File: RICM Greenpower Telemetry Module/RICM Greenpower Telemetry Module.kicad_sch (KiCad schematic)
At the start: 43 parts, among them J1 Conn_02x04_Counter_Clockwise, J10 Conn_01x02_Female, J11 Conn_01x02_Female, J2 Conn_01x05_Female, J3 Conn_01x02_Female, J4 Conn_01x03_Female, J5 Jack-DC, J6 Conn_01x03_Female, J7 Conn_01x04_Female, J8 Conn_01x02_Female, J9 Conn_01x02_Female, U1 MPU_6050_module, U2 Pico, U3 Adafruit_MicroSD_SPI_SDIO, U4 SI-8050TFE, U5 ADS7830

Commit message: tightened up spacing on the board
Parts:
- removed F1: Polyfuse, Capacitor_THT:C_Disc_D5.0mm_W2.5mm_P5.00mm, symbol Device:Polyfuse
- removed U4: SI-8050TFE, Package_TO_SOT_THT:TO-220-5_P3.4x3.7mm_StaggerOdd_Lead3.8mm_Vertical, symbol Regulator_Switching:SI-8050TFE
- added C1: C, Capacitor_THT:C_Disc_D5.0mm_W2.5mm_P5.00mm, symbol Device:C
- added U1: XL2001E1, Package_SO:SO-8_5.3x6.2mm_P1.27mm, symbol Power_Management:XL2001E1
- renumbered C1 to C2, C2 to C3, C3 to C4, C4 to C5, C5 to C6, J5 to J1, J3 to J11, J1 to J3, J6 to J5, J9 to J6, J11 to J7, J7 to J9, R11 to R10, R12 to R11, R13 to R12, R14 to R13, R18 to R14, R20 to R15, R17 to R16, R6 to R17, R8 to R18, R7 to R19, R9 to R20, R10 to R6, R16 to R7, R19 to R8, R15 to R9, U1 to U3, U3 to U4
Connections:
- net +5V: now also U1.1 (FB)
- net GND: now also U1.7 (GND), U1.8 (GND)
- net at C2.1: now also J1.1, C1.2, U1.4 (VIN)
- net at L1.1: now also U1.5 (SW), U1.6 (SW)
- new net: C1.1, U1.3 (VC)
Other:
- moved on the sheet: C2, C3, J1, L1

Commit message: last revisions before first order
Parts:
- added C7, C8: C, Capacitor_THT:C_Disc_D5.0mm_W2.5mm_P5.00mm, symbol Device:C
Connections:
- net +5V: now also U5.10 (REFin/REFout), C7.1, C8.1
- net GND: now also C7.2, C8.2
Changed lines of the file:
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@@
   (junction (at 137.16 29.21) (diameter 0) (color 0 0 0 0)
   )
+  (junction (at 187.96 121.92) (diameter 0) (color 0 0 0 0)
+  )
   (junction (at 33.02 146.05) (diameter 0) (color 0 0 0 0)
   )
@@
   (junction (at 55.88 143.51) (diameter 0) (color 0 0 0 0)
   )
+  (junction (at 200.66 152.4) (diameter 0) (color 0 0 0 0)
+  )
+  (junction (at 209.55 144.78) (diameter 0) (color 0 0 0 0)
+  )
   (junction (at 78.74 91.44) (diameter 0) (color 0 0 0 0)
   )
@@
   (junction (at 138.43 116.84) (diameter 0) (color 0 0 0 0)
   )
+  (junction (at 218.44 137.16) (diameter 0) (color 0 0 0 0)
+  )
   (junction (at 58.42 151.13) (diameter 0) (color 0 0 0 0)
   )
@@
   (junction (at 107.95 53.34) (diameter 0) (color 0 0 0 0)
   )
+  (junction (at 209.55 137.16) (diameter 0) (color 0 0 0 0)
+  )
   (junction (at 67.31 66.04) (diameter 0) (color 0 0 0 0)
   )
@@
     (stroke (width 0) (type default) (color 0 0 0 0))
   )
+  (wire (pts (xy 209.55 144.78) (xy 218.44 144.78))
+    (stroke (width 0) (type default) (color 0 0 0 0))
+  )
   (wire (pts (xy 59.69 71.12) (xy 69.85 71.12))
     (stroke (width 0) (type default) (color 0 0 0 0))
@@
     (stroke (width 0) (type default) (color 0 0 0 0))
   )
+  (wire (pts (xy 209.55 144.78) (xy 209.55 152.4))
+    (stroke (width 0) (type default) (color 0 0 0 0))
+  )
   (wire (pts (xy 67.31 66.04) (xy 67.31 53.34))
     (stroke (width 0) (type default) (color 0 0 0 0))
@@
     (stroke (width 0) (type default) (color 0 0 0 0))
   )
+  (wire (pts (xy 218.44 121.92) (xy 218.44 137.16))
+    (stroke (width 0) (type default) (color 0 0 0 0))
+  )
   (wire (pts (xy 35.56 133.35) (xy 35.56 143.51))
     (stroke (width 0) (type default) (color 0 0 0 0))
@@
     (stroke (width 0) (type default) (color 0 0 0 0))
   )
+  (wire (pts (xy 209.55 152.4) (xy 200.66 152.4))
+    (stroke (width 0) (type default) (color 0 0 0 0))
+  )
   (wire (pts (xy 163.83 100.33) (xy 163.83 127))
     (stroke (width 0) (type default) (color 0 0 0 0))
@@
     (stroke (width 0) (type default) (color 0 0 0 0))
   )
+  (wire (pts (xy 200.66 137.16) (xy 209.55 137.16))
+    (stroke (width 0) (type default) (color 0 0 0 0))
+  )
   (wire (pts (xy 78.74 109.22) (xy 78.74 113.03))
     (stroke (width 0) (type default) (color 0 0 0 0))
@@
     (stroke (width 0) (type default) (color 0 0 0 0))
   )
+  (wire (pts (xy 187.96 121.92) (xy 218.44 121.92))
+    (stroke (width 0) (type default) (color 0 0 0 0))
+  )
   (wire (pts (xy 25.4 30.48) (xy 39.37 30.48))
     (stroke (width 0) (type default) (color 0 0 0 0))
@@
   )
   (wire (pts (xy 58.42 138.43) (xy 58.42 140.97))
+    (stroke (width 0) (type default) (color 0 0 0 0))
+  )
+  (wire (pts (xy 209.55 137.16) (xy 218.44 137.16))
     (stroke (width 0) (type default) (color 0 0 0 0))
   )
@@
     (pin "2")
   )
+  (symbol (lib_id "Device:C") (at 218.44 140.97 0) (unit 1)
+    (in_bom yes) (on_board yes) (fields_autoplaced)
+    (property "Reference" "C8" (id 0) (at 222.25 139.6999 0)
+      (effects (font (size 1.27 1.27)) (justify left))
+    )
+    (property "Value" "C" (id 1) (at 222.25 142.2399 0)
+      (effects (font (size 1.27 1.27)) (justify left))
+    )
+    (property "Footprint" "Capacitor_THT:C_Disc_D5.0mm_W2.5mm_P5.00mm" (id 2) (at 219.4052 144.78 0)
+      (effects (font (size 1.27 1.27)) hide)
+    )
+    (property "Datasheet" "~" (id 3) (at 218.44 140.97 0)
+      (effects (font (size 1.27 1.27)) hide)
+    )
+    (pin "1")
+    (pin "2")
+  )
   (symbol (lib_id "Connector:Conn_01x03_Female") (at 66.04 93.98 180) (unit 1)
     (in_bom yes) (on_board yes) (fields_autoplaced)
@@
     (pin "1")
   )
+  (symbol (lib_id "Device:C") (at 209.55 140.97 0) (unit 1)
+    (in_bom yes) (on_board yes) (fields_autoplaced)
+    (property "Reference" "C7" (id 0) (at 213.36 139.6999 0)
+      (effects (font (size 1.27 1.27)) (justify left))
+    )
+    (property "Value" "C" (id 1) (at 213.36 142.2399 0)
+      (effects (font (size 1.27 1.27)) (justify left))
+    )
+    (property "Footprint" "Capacitor_THT:C_Disc_D5.0mm_W2.5mm_P5.00mm" (id 2) (at 210.5152 144.78 0)
+      (effects (font (size 1.27 1.27)) hide)
+    )
+    (property "Datasheet" "~" (id 3) (at 209.55 140.97 0)
+      (effects (font (size 1.27 1.27)) hide)
+    )
+    (pin "1")
+    (pin "2")
+  )
   (symbol (lib_id "Power_Management:XL2001E1") (at 46.99 142.24 0) (unit 1)
     (in_bom yes) (on_board yes) (fields_autoplaced)
@@
       (effects (font (size 1.27 1.27)) hide)
     )
+    (pin "1")
+    (pin "2")
+    (pin "3")
+    (pin "4")
     (pin "5")
     (pin "6")
-    (pin "1")
-    (pin "2")
-    (pin "3")
-    (pin "4")
     (pin "7")
     (pin "8")
@@
       (reference "C6") (unit 1) (value "47n") (footprint "Capacitor_THT:C_Disc_D4.7mm_W2.5mm_P5.00mm")
     )
+    (path "/9f034d93-2b49-410a-a4b2-29d9d5e1f5cf"
+      (reference "C7") (unit 1) (value "C") (footprint "Capacitor_THT:C_Disc_D5.0mm_W2.5mm_P5.00mm")
+    )
+    (path "/953273d3-9b50-4041-82b2-68427abdf615"
+      (reference "C8") (unit 1) (value "C") (footprint "Capacitor_THT:C_Disc_D5.0mm_W2.5mm_P5.00mm")
+    )
     (path "/1da370c3-b430-46b6-913d-9f5190f2e4da"

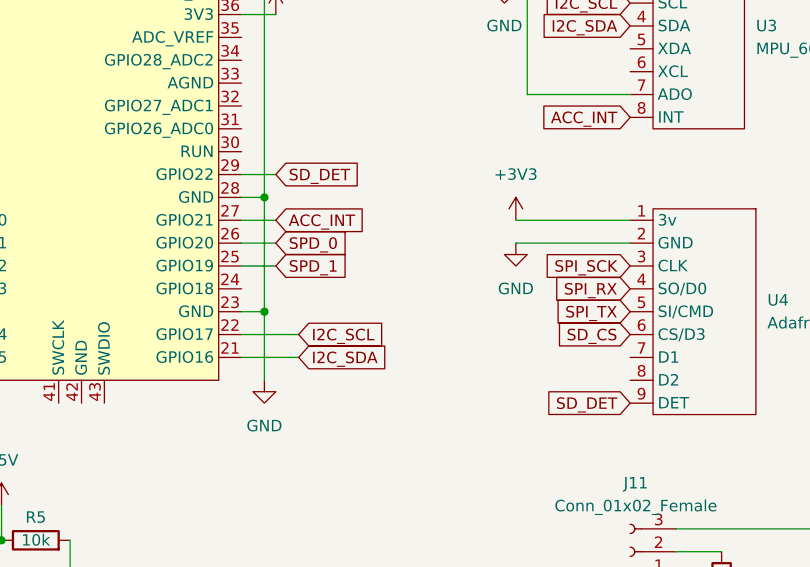
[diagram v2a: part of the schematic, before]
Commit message: Added pullups for i2c
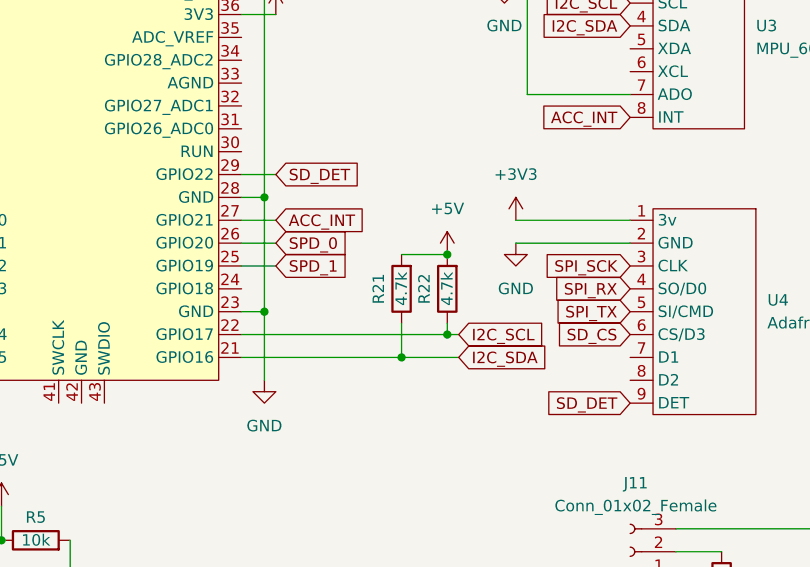
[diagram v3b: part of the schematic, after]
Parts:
- added R21, R22: 4.7k, Resistor_THT:R_Axial_DIN0207_L6.3mm_D2.5mm_P7.62mm_Horizontal, symbol Device:R
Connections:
- net +5V: now also R21.2, R22.2
- net I2C_SCL: now also R22.1
- net I2C_SDA: now also R21.1
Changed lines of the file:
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@@
   (junction (at 140.97 148.59) (diameter 0) (color 0 0 0 0)
   )
+  (junction (at 123.19 71.12) (diameter 0) (color 0 0 0 0)
+  )
   (junction (at 158.75 100.33) (diameter 0) (color 0 0 0 0)
   )
@@
   (junction (at 156.21 107.95) (diameter 0) (color 0 0 0 0)
   )
+  (junction (at 128.27 59.69) (diameter 0) (color 0 0 0 0)
+  )
   (junction (at 33.02 151.13) (diameter 0) (color 0 0 0 0)
   )
@@
   (junction (at 152.4 175.26) (diameter 0) (color 0 0 0 0)
   )
+  (junction (at 128.27 68.58) (diameter 0) (color 0 0 0 0)
+  )
   (junction (at 130.81 116.84) (diameter 0) (color 0 0 0 0)
   )
@@
     (stroke (width 0) (type default) (color 0 0 0 0))
   )
+  (wire (pts (xy 128.27 68.58) (xy 129.54 68.58))
+    (stroke (width 0) (type default) (color 0 0 0 0))
+  )
   (wire (pts (xy 138.43 116.84) (xy 147.32 116.84))
     (stroke (width 0) (type default) (color 0 0 0 0))
@@
     (stroke (width 0) (type default) (color 0 0 0 0))
   )
-  (wire (pts (xy 105.41 68.58) (xy 111.76 68.58))
-    (stroke (width 0) (type default) (color 0 0 0 0))
-  )
   (wire (pts (xy 31.75 140.97) (xy 31.75 146.05))
     (stroke (width 0) (type default) (color 0 0 0 0))
@@
     (stroke (width 0) (type default) (color 0 0 0 0))
   )
+  (wire (pts (xy 105.41 71.12) (xy 123.19 71.12))
+    (stroke (width 0) (type default) (color 0 0 0 0))
+  )
   (wire (pts (xy 163.83 100.33) (xy 163.83 127))
     (stroke (width 0) (type default) (color 0 0 0 0))
@@
     (stroke (width 0) (type default) (color 0 0 0 0))
   )
+  (wire (pts (xy 128.27 67.31) (xy 128.27 68.58))
+    (stroke (width 0) (type default) (color 0 0 0 0))
+  )
   (wire (pts (xy 33.02 151.13) (xy 33.02 152.4))
     (stroke (width 0) (type default) (color 0 0 0 0))
@@
     (stroke (width 0) (type default) (color 0 0 0 0))
   )
+  (wire (pts (xy 123.19 59.69) (xy 128.27 59.69))
+    (stroke (width 0) (type default) (color 0 0 0 0))
+  )
   (wire (pts (xy 52.07 35.56) (xy 69.85 35.56))
     (stroke (width 0) (type default) (color 0 0 0 0))
@@
     (stroke (width 0) (type default) (color 0 0 0 0))
   )
+  (wire (pts (xy 105.41 68.58) (xy 128.27 68.58))
+    (stroke (width 0) (type default) (color 0 0 0 0))
+  )
   (wire (pts (xy 123.19 111.76) (xy 123.19 114.3))
     (stroke (width 0) (type default) (color 0 0 0 0))
   )
-  (wire (pts (xy 105.41 71.12) (xy 111.76 71.12))
-    (stroke (width 0) (type default) (color 0 0 0 0))
-  )
   (wire (pts (xy 58.42 138.43) (xy 58.42 140.97))
     (stroke (width 0) (type default) (color 0 0 0 0))
@@
     (stroke (width 0) (type default) (color 0 0 0 0))
   )
+  (wire (pts (xy 123.19 71.12) (xy 129.54 71.12))
+    (stroke (width 0) (type default) (color 0 0 0 0))
+  )
   (wire (pts (xy 67.31 27.94) (xy 69.85 27.94))
     (stroke (width 0) (type default) (color 0 0 0 0))
@@
   )
   (wire (pts (xy 95.25 166.37) (xy 101.6 166.37))
+    (stroke (width 0) (type default) (color 0 0 0 0))
+  )
+  (wire (pts (xy 123.19 67.31) (xy 123.19 71.12))
     (stroke (width 0) (type default) (color 0 0 0 0))
   )
@@
     )
   )
-  (global_label "I2C_SCL" (shape input) (at 111.76 68.58 0) (fields_autoplaced)
+  (global_label "I2C_SCL" (shape input) (at 129.54 68.58 0) (fields_autoplaced)
     (effects (font (size 1.27 1.27)) (justify left))
-    (property "Intersheet References" "${INTERSHEET_REFS}" (id 0) (at 121.7326 68.6594 0)
+    (property "Intersheet References" "${INTERSHEET_REFS}" (id 0) (at 139.5126 68.6594 0)
       (effects (font (size 1.27 1.27)) (justify left) hide)
     )
@@
     )
   )
-  (global_label "I2C_SDA" (shape input) (at 111.76 71.12 0) (fields_autoplaced)
+  (global_label "I2C_SDA" (shape input) (at 129.54 71.12 0) (fields_autoplaced)
     (effects (font (size 1.27 1.27)) (justify left))
-    (property "Intersheet References" "${INTERSHEET_REFS}" (id 0) (at 121.7931 71.1994 0)
+    (property "Intersheet References" "${INTERSHEET_REFS}" (id 0) (at 139.5731 71.1994 0)
       (effects (font (size 1.27 1.27)) (justify left) hide)
     )
@@
     (pin "5")
   )
+  (symbol (lib_id "Device:R") (at 123.19 63.5 180) (unit 1)
+    (in_bom yes) (on_board yes)
+    (property "Reference" "R21" (id 0) (at 120.65 63.5 90))
+    (property "Value" "4.7k" (id 1) (at 123.19 63.5 90))
+    (property "Footprint" "Resistor_THT:R_Axial_DIN0207_L6.3mm_D2.5mm_P7.62mm_Horizontal" (id 2) (at 124.968 63.5 90)
+      (effects (font (size 1.27 1.27)) hide)
+    )
+    (property "Datasheet" "~" (id 3) (at 123.19 63.5 0)
+      (effects (font (size 1.27 1.27)) hide)
+    )
+    (pin "1")
+    (pin "2")
+  )
   (symbol (lib_id "power:GND") (at 180.34 107.95 0) (unit 1)
     (in_bom yes) (on_board yes) (fields_autoplaced)
@@
     )
     (pin "1")
+  )
+  (symbol (lib_id "Device:R") (at 128.27 63.5 180) (unit 1)
+    (in_bom yes) (on_board yes)
+    (property "Reference" "R22" (id 0) (at 125.73 63.5 90))
+    (property "Value" "4.7k" (id 1) (at 128.27 63.5 90))
+    (property "Footprint" "Resistor_THT:R_Axial_DIN0207_L6.3mm_D2.5mm_P7.62mm_Horizontal" (id 2) (at 130.048 63.5 90)
+      (effects (font (size 1.27 1.27)) hide)
+    )
+    (property "Datasheet" "~" (id 3) (at 128.27 63.5 0)
+      (effects (font (size 1.27 1.27)) hide)
+    )
+    (pin "1")
+    (pin "2")
   )
   (symbol (lib_id "Device:R") (at 152.4 171.45 0) (unit 1)
@@
     (pin "2")
   )
+  (symbol (lib_id "power:+5V") (at 128.27 59.69 0) (unit 1)
+    (in_bom yes) (on_board yes) (fields_autoplaced)
+    (property "Reference" "#PWR035" (id 0) (at 128.27 63.5 0)
+      (effects (font (size 1.27 1.27)) hide)
+    )
+    (property "Value" "+5V" (id 1) (at 128.27 54.61 0))
+    (property "Footprint" "" (id 2) (at 128.27 59.69 0)
+      (effects (font (size 1.27 1.27)) hide)
+    )
+    (property "Datasheet" "" (id 3) (at 128.27 59.69 0)
+      (effects (font (size 1.27 1.27)) hide)
+    )
+    (pin "1")
+  )
   (symbol (lib_id "power:+5V") (at 134.62 26.67 0) (unit 1)
     (in_bom yes) (on_board yes) (fields_autoplaced)
@@
       (reference "#PWR034") (unit 1) (value "GND") (footprint "")
     )
+    (path "/e568c9f3-f54f-4a9c-899a-4926c16d9cbc"
+      (reference "#PWR035") (unit 1) (value "+5V") (footprint "")
+    )
     (path "/eeb2398d-f466-4ceb-9eea-4480931c5a1b"
       (reference "C1") (unit 1) (value "C") (footprint "Capacitor_THT:C_Disc_D5.0mm_W2.5mm_P5.00mm")
@@
       (reference "R20") (unit 1) (value "10k") (footprint "Resistor_THT:R_Axial_DIN0207_L6.3mm_D2.5mm_P7.62mm_Horizontal")
     )
+    (path "/251805a9-5d75-4731-b6bc-fd009a038646"
+      (reference "R21") (unit 1) (value "4.7k") (footprint "Resistor_THT:R_Axial_DIN0207_L6.3mm_D2.5mm_P7.62mm_Horizontal")
+    )
+    (path "/606c7fb4-9629-4beb-a324-23c1e0199ea0"
+      (reference "R22") (unit 1) (value "4.7k") (footprint "Resistor_THT:R_Axial_DIN0207_L6.3mm_D2.5mm_P7.62mm_Horizontal")
+    )
     (path "/a0525f4b-32be-4e90-8496-5b7e608a9b2d"
